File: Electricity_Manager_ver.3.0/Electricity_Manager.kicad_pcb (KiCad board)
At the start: 2 copper layers, 100 x 77 mm, 196 parts, among them IC2 MAIN_SHUTDOWN, IC3 RELAY_STATE, IC4 ADC_RST, J1 SERIAL, P1 SWD, P10 EMERGENCY, P11 EMERGENCY, P12 FRAME_GRAND, P13 BATT_IN, P15 OUT_B, P16 BATT_IN, P17 OUT_A, P2 CAN, P3 CAN, P4 EMERGENCY_SIGNAL, P5 EMERGENCY_SIGNAL, P6 12V_OUT, P7 12V_OUT, P8 MAIN_~RST, P9 MAIN_SW, Q1 FET_N, Q2 NPN, Q3 NPN, Q4 FET_N, Q7 FET_N, SW1 RST, SW2 SW0, SW3 SW1, U1 MAX3051, U10 BD9G101G, U11 OUTA_CHECK, U12 V23134J1052D642, U13 ACS70331, U14 OUTB_CHECK, U15 BD33FA1, U16 LOGO, U17 LOGO, U18 LOGO, U19 MCP2221A, U2 STM32F405RG, U20 OSRB38C9AA, U21 OSRB38C9AA, U22 HSIN_946, U23 LOGO, U24 LOGO, U25 LOGO, U3 FULL COLOR, U4 AQM0802_BL, U5 AP3211, U6 SI8900, U7 AZ1086H, U8 V23134J1052D642, U9 RPA60-12FW/N, X1 8MHz

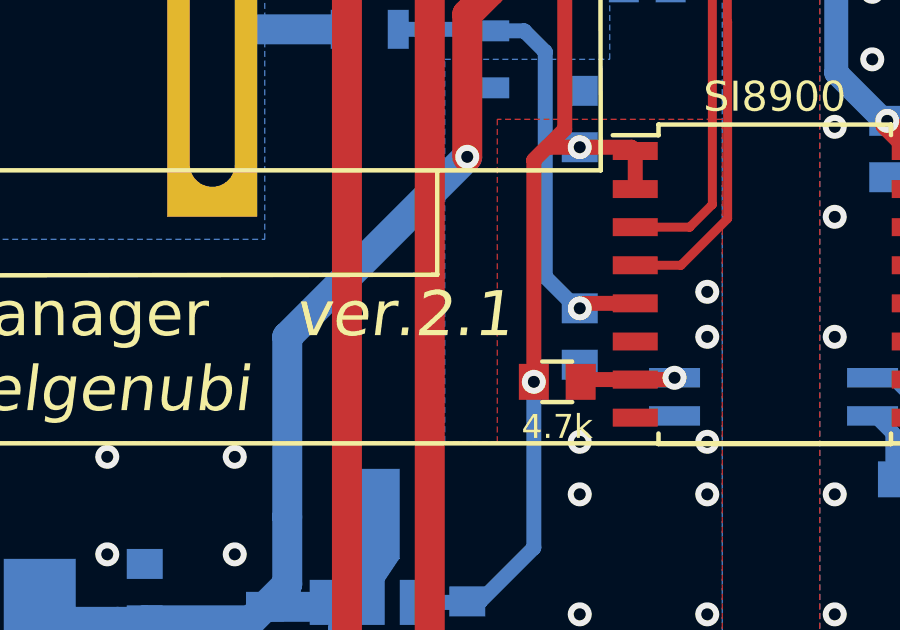
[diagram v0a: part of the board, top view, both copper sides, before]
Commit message: 電源基板のシルク表記を直しただけ
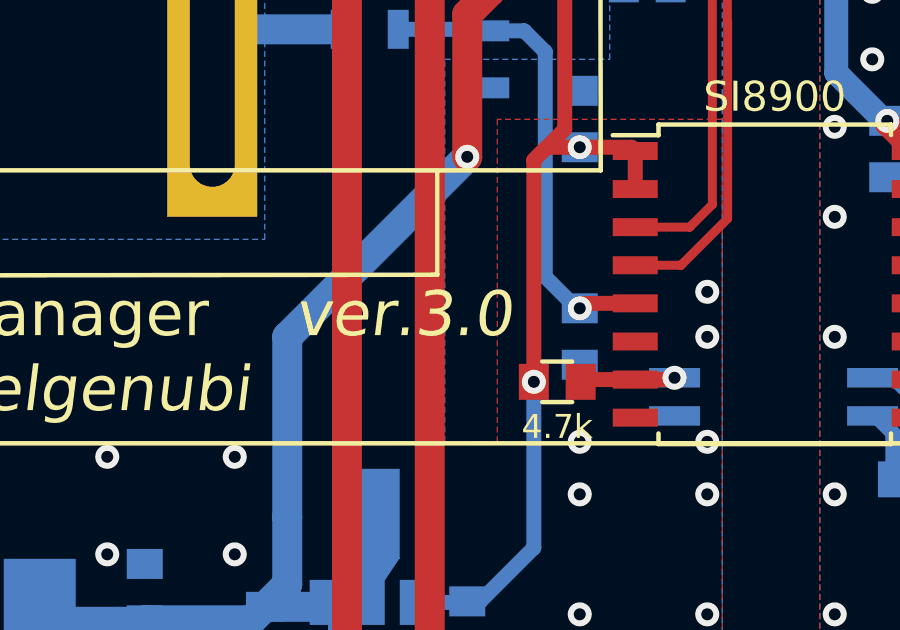
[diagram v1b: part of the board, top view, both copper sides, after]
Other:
- board text added: "ver.3.0"
- board text removed: "ver.2.1"
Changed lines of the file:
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@@
       (drillshape 0)
       (scaleselection 1)
-      (outputdirectory "C:/Users/3Zuta/Documents/NHK_RC20_PCBs/Electricity_Manager_ver.2.1/加工/"))
+      (outputdirectory "C:/Users/3Zuta/Documents/NHK_RC20_PCBs/Electricity_Manager_ver.3.0/加工/"))
   )
   (net 0 "")
@@
     )
   )
-  (gr_text ver.2.1 (at 92 145) (layer F.SilkS)
+  (gr_text ver.3.0 (at 92 145) (layer F.SilkS)
     (effects (font (size 1.5 1.5) (thickness 0.375) italic) (justify left))
   )

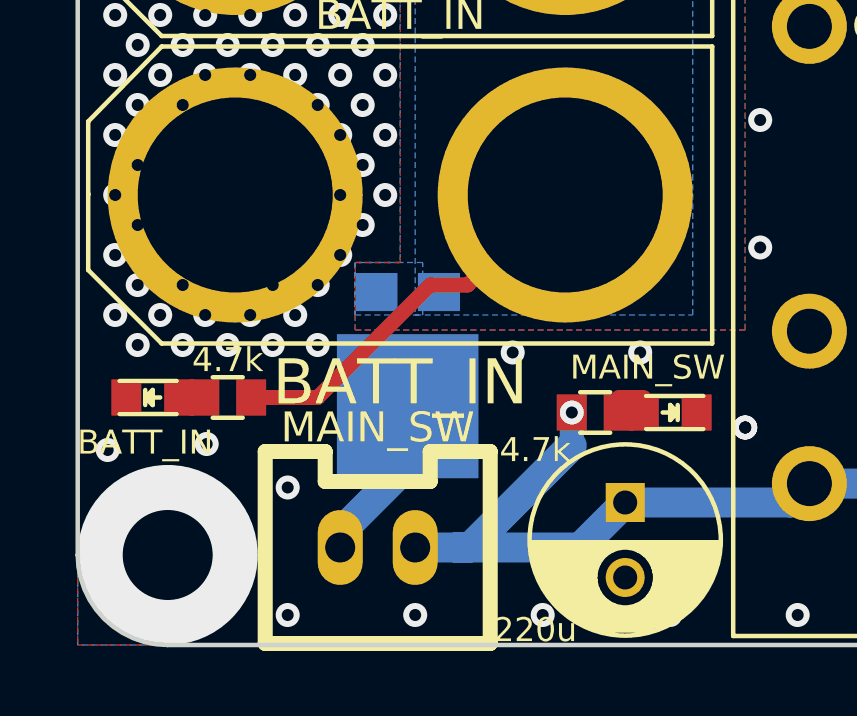
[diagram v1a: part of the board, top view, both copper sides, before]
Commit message: 電源基板ver.3.0の3D化&修正
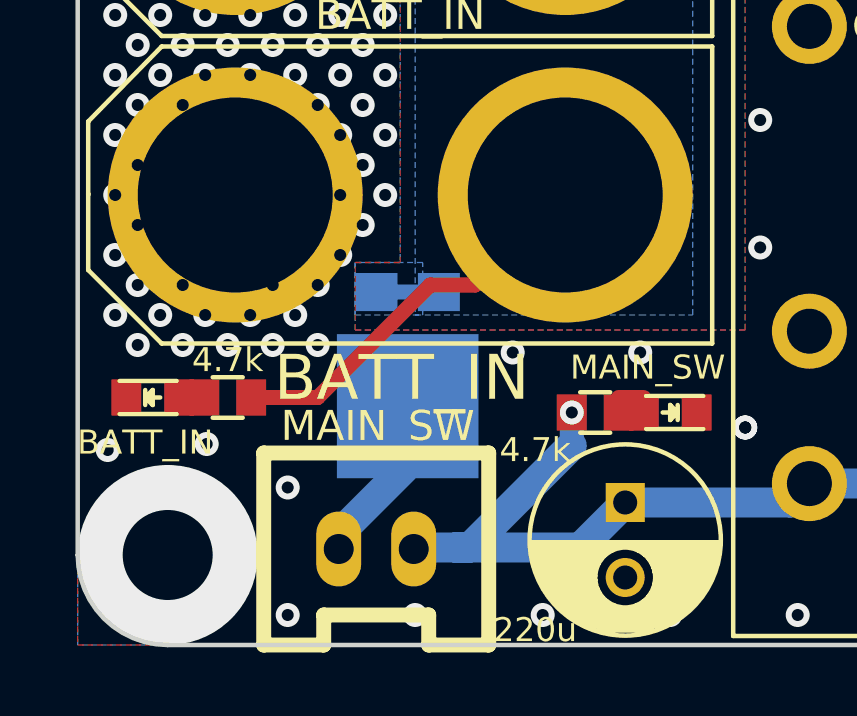
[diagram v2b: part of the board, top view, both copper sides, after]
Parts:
- moved P9 2.55 mm to (56.7, 171.8), turned to 0 degrees
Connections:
- P9 pad 1: Net-(D10-Pad3) -> /24V
- P9 pad 2: /24V -> Net-(D10-Pad3)
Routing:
- net +BATT: track 17.7 -> 19.6 mm
